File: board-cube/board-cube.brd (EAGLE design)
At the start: 100 x 100 mm, 164 parts, among them IC1 MSP430FR2110PW, IC2 LHA1+, IC3 MMZ09332BT1, Q1 BSS84, U1 TPS79933QDDCRQ1, U2 TPS79933QDDCRQ1, X1 BU-SMA-V, X10 BU-SMA-V, X11 BU-SMA-V, X12 BU-SMA-V, X13 BU-SMA-V, X14 BU-SMA-V, X15 BU-SMA-V, X16 BU-SMA-V, X17 BU-SMA-V, X2 BU-SMA-V, X3 BU-SMA-V, X4 BU-SMA-V, X5 BU-SMA-V, X6 BU-SMA-V, X7 BU-SMA-V, X8 BU-SMA-V, X9 BU-SMA-V

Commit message: adding tcxo and temp sensor
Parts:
- added C76, C77: 10n, passives-7351:C0603-N
- added C78, C79, C80, C81: 100n, passives-7351:C0603-N
- added IC4, IC5: PCT2075TP, CubeSat3:HWSON8
- added R20, R21: 4k7, passives-7351:R0603-N
- added TP4, TP5: PTR1B1,27, testpad:B1,27
- added X18, X19: SHIELD-26X26, CubeSat3:SHIELD-26X26
- added X20, X21: LFTCXO070, CubeSat3:260-SERIES
- moved C63 2.04 mm to (48.5, 24.6)
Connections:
- new net N$81: C76.1, X20.4
- new net N$82: C77.1, X21.4
- new net N$86: C78.1, C79.1, IC4.8, IC5.7, IC5.8, R20.2, R21.2
- new net SCL: IC4.2, IC5.2, R21.1, TP5.TP
- new net SDA: IC4.1, IC5.1, R20.1, TP4.TP
- net GND: now also C78.2, C79.2, C80.2, C81.2, IC4.4, IC4.5, IC4.6, IC4.7, IC4.EP, IC5.4, IC5.5, IC5.6, IC5.EP, X18.G1, X18.G10, X18.G11, X18.G12, X18.G13, X18.G14, X18.G15, X18.G16, X18.G17, X18.G19, X18.G2, X18.G20, X18.G21, X18.G3, X18.G4, X18.G5, X18.G6, X18.G7, X18.G8, X18.G9, X19.G1, X19.G10, X19.G11, X19.G12, X19.G13, X19.G14, X19.G15, X19.G16, X19.G17, X19.G19, X19.G2, X19.G20, X19.G21, X19.G3, X19.G4, X19.G5, X19.G6, X19.G7, X19.G8, X19.G9, X20.1, X20.3, X21.1, X21.3
- net N$36: now also C77.2
- net N$51: now also C80.1, X20.6
- net N$63: now also C81.1, X21.6
- net N$9: now also C76.2

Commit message: updating footprints and values, changing msp watchdog part
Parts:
- removed IC1: MSP430FR2110PW, CubeSat3:SSOP16
- removed U$1, U$4: CC1125RHBT, cube-parts:QFN50P500X500X100-32N
- added C82: (no value), passives-7351:C0603-N
- added IC6: MSP430FR2311PW, CubeSat3:SSOP16
- added IC7, IC8: CC1125RHBT, cube-parts:QFN32_5X5
- added JP11: FTDI_BASICPTH, SparkFun-Connectors:FTDI_BASIC
- added JP8: (no value), SparkFun-Connectors:1X04
- added L21: 15n, passives-7351:L0603-N
- C60: value (none) -> 12p
- moved X1 18.9 mm to (23.1, 37.8)
- moved C21 8.94 mm to (19.2, 27.4), turned to 0 degrees
- moved L4 6.45 mm to (19.2, 29.0), turned to 0 degrees
- moved C19 5.98 mm to (22.9, 25.9), turned to 0 degrees
- moved C22 5.38 mm to (17.0, 25.2), turned to 90 degrees
- moved C18 3.95 mm to (22.9, 24.2), turned to 0 degrees
- moved L3 2.88 mm to (16.0, 27.4), turned to 0 degrees
- moved X20 2.00 mm to (4.40, 9.60)
- moved C1 2.00 mm to (9.25, 21.8)
- moved C10 2.00 mm to (13.8, 9.25)
- moved C11 2.00 mm to (11.2, 10.0)
- moved C12 2.00 mm to (4.00, 12.0)
- moved C13 2.00 mm to (4.00, 13.5)
- moved C14 2.00 mm to (10.8, 21.8)
- moved C15 2.00 mm to (4.00, 15.0)
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- renumbered U$3 to FL1, U$6 to FL2, U$7 to FL3
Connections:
- new net N$83: IC6.3, JP8.4
- new net N$84: IC6.4, JP8.3
- new net N$85: IC6.11, JP11.TXO
- new net N$87: IC6.10, JP11.RXI
- new net N$88: C82.1, L21.2
- new net N$89: L21.1
- new net N$90: C82.2
- net GND: now also IC6.6, IC7.19, IC7.20, IC7.30, IC7.33, IC8.30, IC8.33, JP11.GND, JP8.2; no longer IC1.6, U$1.19, U$1.20, U$1.30, U$1.33, U$4.30, U$4.33
- net N$1: now also IC7.23; no longer U$1.23
- net N$13: now also IC7.18; no longer U$1.18
- net N$19: now also IC7.6; no longer U$1.6
- net N$2: now also IC7.24; no longer U$1.24
- net N$21: now also C60.2
- net N$30: now also IC8.23; no longer U$4.23
- net N$31: now also IC8.24; no longer U$4.24
- net N$32: now also IC8.21; no longer U$4.21
- net N$35: now also IC8.14; no longer U$4.14
- net N$36: now also IC8.32; no longer U$4.32
- net N$4: now also IC7.21; no longer U$1.21
- net N$45: now also IC8.6; no longer U$4.6
- net N$47: now also IC8.19; no longer U$4.19
- net N$48: now also IC8.20; no longer U$4.20
- net N$51: now also IC7.1, IC7.12, IC7.13, IC7.15, IC7.22, IC7.25, IC7.26, IC7.27, IC7.28, IC7.29, IC7.5; no longer U$1.1, U$1.12, U$1.13, U$1.15, U$1.22, U$1.25, U$1.26, U$1.27, U$1.28, U$1.29, U$1.5
- net N$63: now also IC8.1, IC8.12, IC8.13, IC8.15, IC8.22, IC8.25, IC8.26, IC8.27, IC8.28, IC8.29, IC8.5; no longer U$4.1, U$4.12, U$4.13, U$4.15, U$4.22, U$4.25, U$4.26, U$4.27, U$4.28, U$4.29, U$4.5
- net N$7: now also IC7.17; no longer U$1.17
- net N$8: now also IC7.14; no longer U$1.14
- net N$80: now also IC6.5, JP8.1; no longer IC1.5
- net N$9: now also IC7.32; no longer U$1.32
- net RX_CLK: now also IC8.8; no longer U$4.8
- net RX_CS: now also IC8.11; no longer U$4.11
- net RX_GPIO0: now also IC8.10; no longer U$4.10
- net RX_GPIO2: now also IC8.4; no longer U$4.4
- net RX_GPIO3: now also IC8.3; no longer U$4.3
- net RX_MISO: now also IC8.9; no longer U$4.9
- net RX_MOSI: now also IC8.7; no longer U$4.7
- net RX_RST: now also IC8.2; no longer U$4.2
- net SCL: now also IC6.15
- net SDA: now also IC6.16
- net TX_CLK: now also IC7.8; no longer U$1.8
- net TX_CS: now also IC7.11; no longer U$1.11
- net TX_GPIO0: now also IC7.10; no longer U$1.10
- net TX_GPIO2: now also IC7.4; no longer U$1.4
- net TX_GPIO3: now also IC7.3; no longer U$1.3
- net TX_MISO: now also IC7.9; no longer U$1.9
- net TX_MOSI: now also IC7.7; no longer U$1.7
- net TX_RST: now also IC7.2; no longer U$1.2
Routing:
- net TX_MISO: track 22.2 -> 20.2 mm
- net TX_GPIO3: track 30.3 -> 28.3 mm
- net TX_CLK: track 58.3 -> 56.3 mm
- net TX_GPIO0: track 23.8 -> 21.8 mm
- net GND: track 11.6 -> 12.9 mm
- net N$22: track 5.71 -> 4.68 mm
- net N$23: track 11.7 -> 12.3 mm

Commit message: added level shifter
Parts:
- removed JP10: (no value), SparkFun-Connectors:2X3
- added C83, C84, C85, C86: 100n, passives-7351:C0603-N
- added IC1, IC9: TXB0108PW, cube-parts:TSSOP20
- added JP12, JP13: M02PTH, SparkFun-Connectors:1X02
- added R22, R23: 10k, passives-7351:R0603-N
- added R24: 0.2, passives-7351:R0603-N
- JP9: value (none) -> M02PTH; device SparkFun-Connectors:2X3 -> SparkFun-Connectors:1X02
- moved JP9 633.8 mm to (-299.6, -501.2), turned to 0 degrees
- moved X12 10.1 mm to (60.8, 64.6)
- moved FL3 10.1 mm to (50.5, 64.8)
- moved X11 10.0 mm to (41.2, 64.8)
- moved R4 7.64 mm to (21.9, 63.5)
- moved Q1 6.85 mm to (18.4, 63.8)
- moved C55 4.88 mm to (16.2, 69.3)
- moved C54 4.66 mm to (16.2, 66.9)
- moved X9 2.83 mm to (89.8, 76.2)
- moved X10 2.40 mm to (69.9, 76.6)
- moved FL2 2.00 mm to (80.0, 76.3)
- moved X5 1.60 mm to (51.9, 76.6)
- moved FL1 1.26 mm to (41.4, 77.0)
- moved X3 0.89 mm to (30.5, 77.0)
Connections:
- removed net A0_CLK: JP9.3
- removed net A0_CS: JP9.1
- removed net A0_SIMO: JP9.5
- removed net B0_CLK: JP10.3
- removed net B0_CS: JP10.1
- removed net B0_SIMO: JP10.5
- new net N$91: IC9.10, JP13.1, R23.1
- new net N$92: C84.1, IC1.19
- new net N$93: C86.1, IC9.19
- new net N$94: C49.1, JP9.2, R24.2, U1.1, U1.3
- net +5V: now also JP9.1, R24.1; no longer C49.1, U1.1, U1.3
- net GND: now also C83.2, C84.2, C85.2, C86.2, IC1.11, IC9.11, JP12.2, JP13.2
- net N$51: now also C73.1, C74.1, C75.1, C83.1, IC1.2, IC6.5, JP8.1, R22.2
- net N$63: now also C85.1, IC9.2, R23.2
- net N$80: now also IC1.10, JP12.1, R22.1; no longer C73.1, C74.1, C75.1, IC6.5, JP8.1
- net RX_CLK: no longer JP10.4
- net RX_CS: no longer JP10.2
- net RX_MOSI: no longer JP10.6
- net SCL: no longer IC6.15
- net SDA: no longer IC6.16
- net TX_CLK: no longer JP9.4
- net TX_CS: no longer JP9.2
- net TX_MOSI: no longer JP9.6
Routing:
- net TX_CS: track 53.8 -> 19.6 mm
- net N$94: track 0.00 -> 2.75 mm
- net +5V: track 2.75 -> 0.00 mm

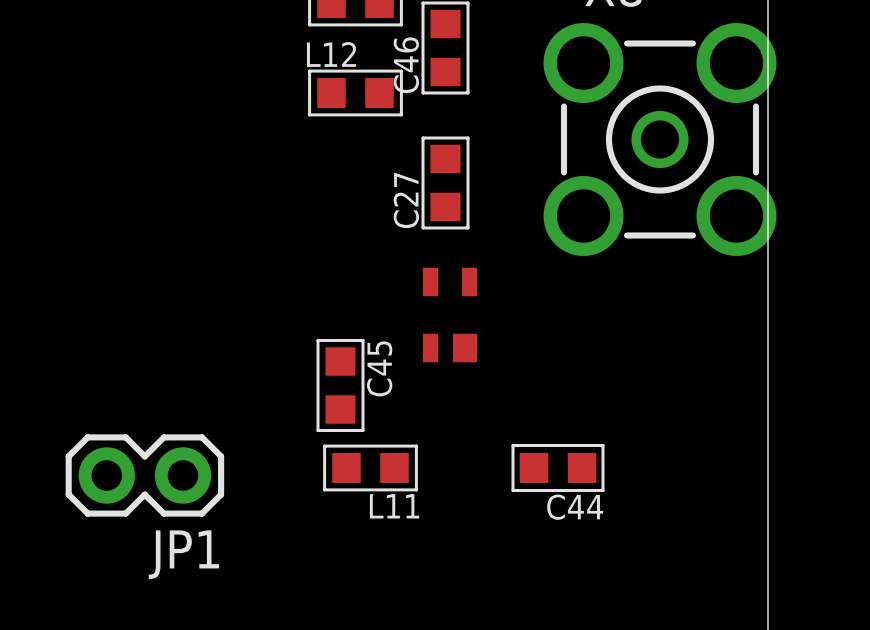
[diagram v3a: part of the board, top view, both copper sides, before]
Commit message: Fix PSA5043 LNA footprint.
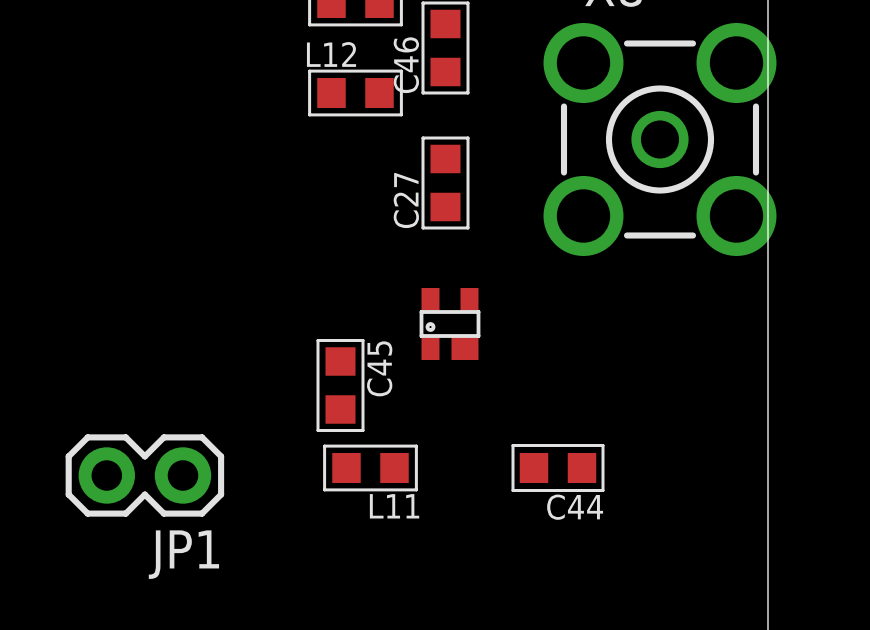
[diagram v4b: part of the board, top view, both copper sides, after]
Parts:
- renumbered U$5 to IC10
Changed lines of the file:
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@@
 <element name="L9" library="passives-7351" package="L0603-N" value="27u" x="91" y="27.25" rot="R90"/>
 <element name="C44" library="passives-7351" package="C0603-N" value="??" x="93" y="51.25" rot="R180"/>
-<element name="U$5" library="CubeSat3" package="LNA_MMM1362" value="LNA_COMMON" x="88.75" y="55.25"/>
+<element name="IC10" library="CubeSat3" package="LNA_MMM1362" value="LNA_COMMON" x="88.75" y="55.25"/>
 <element name="C27" library="passives-7351" package="C0603-N" value="??" x="89.25" y="60.75" rot="R90"/>
 <element name="L11" library="passives-7351" package="L0603-N" value="??" x="86.75" y="51.25" rot="R180"/>
@@
 <contactref element="C43" pad="2"/>
 <contactref element="L8" pad="1"/>
-<contactref element="U$5" pad="4"/>
-<contactref element="U$5" pad="2"/>
+<contactref element="IC10" pad="4"/>
+<contactref element="IC10" pad="2"/>
 <contactref element="C45" pad="1"/>
 <contactref element="L12" pad="1"/>
@@
 <wire x1="85.45" y1="66.75" x2="80.05" y2="72.286" width="0" layer="19" extent="1-1"/>
 <wire x1="85.45" y1="63.75" x2="85.45" y2="66.75" width="0" layer="19" extent="1-1"/>
-<wire x1="88.75" y1="57.45" x2="85.45" y2="63.75" width="0" layer="19" extent="1-1"/>
-<wire x1="89.9" y1="55.25" x2="88.75" y2="57.45" width="0" layer="19" extent="1-1"/>
-<wire x1="85.75" y1="54.8" x2="88.75" y2="57.45" width="0" layer="19" extent="1-1"/>
-<wire x1="93.8501" y1="59.6501" x2="88.75" y2="57.45" width="0" layer="19" extent="1-1"/>
+<wire x1="88.75" y1="56.85" x2="85.45" y2="63.75" width="0" layer="19" extent="1-1"/>
+<wire x1="89.9" y1="55.25" x2="88.75" y2="56.85" width="0" layer="19" extent="1-1"/>
+<wire x1="85.75" y1="54.8" x2="88.75" y2="56.85" width="0" layer="19" extent="1-1"/>
+<wire x1="93.8501" y1="59.6501" x2="88.75" y2="56.85" width="0" layer="19" extent="1-1"/>
 <wire x1="98.9499" y1="59.6501" x2="93.8501" y2="59.6501" width="0" layer="19" extent="1-1"/>
 <wire x1="98.9499" y1="64.7499" x2="98.9499" y2="59.6501" width="0" layer="19" extent="1-1"/>
@@
 <contactref element="L11" pad="1"/>
 <contactref element="C44" pad="2"/>
-<contactref element="U$5" pad="1"/>
+<contactref element="IC10" pad="1"/>
 <wire x1="87.55" y1="51.25" x2="92.2" y2="51.25" width="0" layer="19" extent="1-1"/>
 <wire x1="88.75" y1="55.25" x2="87.55" y2="51.25" width="0" layer="19" extent="1-1"/>
@@
 <signal name="N$46">
 <contactref element="C27" pad="1"/>
-<contactref element="U$5" pad="3"/>
-<wire x1="90.05" y1="57.45" x2="89.25" y2="59.95" width="0" layer="19" extent="1-1"/>
+<contactref element="IC10" pad="3"/>
+<wire x1="90.05" y1="56.85" x2="89.25" y2="59.95" width="0" layer="19" extent="1-1"/>
 </signal>
 <signal name="N$52">

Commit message: moving things around to fit better
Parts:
- moved IC9 596.1 mm to (71.2, 9.60)
- moved IC1 596.1 mm to (71.2, 17.2)
- moved X7 399.2 mm to (89.3, 82.6)
- moved C63 48.1 mm to (45.2, 72.7)
- moved C68 48.1 mm to (52.8, 64.4)
- moved C61 48.1 mm to (42.8, 66.8)
- moved C62 48.1 mm to (38.9, 69.0)
- moved C64 48.1 mm to (42.0, 58.4)
- moved C65 48.1 mm to (42.0, 60.0)
- moved C66 48.1 mm to (46.0, 63.2)
- moved C67 48.1 mm to (45.2, 60.8)
- moved C69 48.1 mm to (48.8, 60.8)
- moved IC3 48.1 mm to (47.8, 66.5)
- moved IC5 48.1 mm to (48.4, 72.8)
- moved L10 48.1 mm to (39.6, 66.8)
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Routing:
- net TX_CLK: track 56.3 -> 16.3 mm, vias 3 -> 2
- net RX_MISO: track 36.5 -> 0.00 mm, vias 1 -> 0
- net A1_TX: track 31.0 -> 0.00 mm
- net RX_MOSI: track 30.9 -> 0.00 mm, vias 2 -> 0
- net N$63: track 15.6 -> 0.00 mm
- net TX_RST: track 41.7 -> 28.5 mm
- net N$49: track 11.2 -> 0.00 mm
- net TX_GPIO0: track 21.8 -> 11.5 mm
- net RX_CS: track 8.98 -> 0.00 mm
- net N$47: track 8.18 -> 0.00 mm
- net RX_GPIO0: track 8.13 -> 0.00 mm
- net TX_CS: track 19.6 -> 11.7 mm
- net N$48: track 7.23 -> 0.00 mm
- net A1_RX: track 6.76 -> 0.00 mm
- net TX_GPIO3: track 28.3 -> 23.3 mm
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
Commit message: most digital signals wired up
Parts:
- removed X13: BU-SMA-V, con-coax:BU-SMA-V
- added C87: 100n, passives-7351:C0603-N
- added Q2: BSS123, transistor-small-signal:SOT23
- added Q3: BSS84, transistor-small-signal:SOT23
- added R25: 10k, passives-7351:R0603-N
- added R26: 100k, passives-7351:R0603-N
- added TP6: PTR1B1,27, testpad:B1,27
- added U3: 74LVC1G08, SparkFun-DigitalIC:SOT23-5
- JP5: value FTDI_BASICPTH -> M02PTH; device SparkFun-Connectors:FTDI_BASIC -> SparkFun-Connectors:1X02
- R18: value 4k7 -> 10k
- TP1, TP2, TP3: value PTR1PAD1-20 -> PTR1B1,27; device testpad:P1-20 -> testpad:B1,27
- U1, U2: value TPS79933QDDCRQ1 -> TPS79930QDDCRQ1
- moved R23 621.8 mm to (62.4, 9.20), turned to 90 degrees
- moved JP12 617.9 mm to (65.6, 15.6), turned to 90 degrees
- moved JP13 617.6 mm to (65.2, 8.00), turned to 90 degrees
- moved R22 616.6 mm to (62.8, 20.8), turned to 90 degrees
- moved JP11 615.4 mm to (94.4, 34.8), turned to 90 degrees
- moved C83 612.4 mm to (70.4, 22.8)
- moved C84 611.4 mm to (66.0, 21.6), turned to 90 degrees
- moved R24 607.6 mm to (30.0, 3.20), turned to 90 degrees
- moved C85 600.3 mm to (67.2, 3.60)
- moved C86 600.2 mm to (62.8, 3.60)
- moved JP9 599.7 mm to (27.2, 1.60), turned to 90 degrees
- moved C82 593.4 mm to (55.2, 28.8), turned to 90 degrees
- moved C79 590.3 mm to (48.4, 76.0)
- moved L21 588.2 mm to (52.4, 28.0)
- moved JP8 587.8 mm to (38.0, 51.6), turned to 180 degrees
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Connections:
- removed net +3V3: JP5.VCC
- removed net A1_RX: JP5.TXO
- removed net A1_TX: JP5.RXI
- removed net N$89: L21.1
- new net N$101: IC9.12
- new net N$102: IC1.20
- new net N$103: IC1.18
- new net N$104: IC1.17
- new net N$105: IC1.16
- new net N$106: IC1.15
- new net N$107: IC1.14
- new net N$108: IC1.13
- new net N$109: IC1.12
- new net N$110: IC9.13
- new net N$111: IC9.14
- new net N$112: IC9.15
- new net N$113: IC9.16
- new net N$114: IC9.17
- new net N$115: IC9.18
- new net N$116: IC9.20
- new net N$117: Q2.1, R18.2, U3.4
- new net WDT_ACK: IC6.13
- new net WDT_ERR: IC1.9, IC6.14
- new net WDT_PA_EN: IC6.2, TP6.TP, U3.2
- net +5V: now also JP7.1
- net GND: now also C87.2, IC3.10, Q2.2, U3.3; no longer JP5.GND
- net N$24: now also LED9.A
- net N$49: now also C82.2; no longer C31.2, L9.2
- net N$51: now also C87.1, U3.5
- net N$52: now also JP5.2
- net N$53: now also JP5.1, Q3.2, R26.2; no longer JP1.2
- net N$6: now also JP7.2
- net N$62: now also Q2.3; no longer JP7.1
- net N$69: now also C49.1, JP9.2, R24.2, R25.2, U1.1; no longer JP7.2, R18.2
- net N$75: now also JP1.2, Q3.3; no longer IC3.10
- net N$90: now also C31.2, L21.1, L9.2; no longer C82.2
- net N$94: now also R25.1; no longer C49.1, JP9.2, R24.2, U1.1
- net RX_CLK: now also IC9.7
- net RX_CS: now also IC9.8
- net RX_GPIO0: now also IC9.1; no longer TP3.TP
- net RX_GPIO2: now also IC9.3
- net RX_GPIO3: now also IC9.4, Q3.1, R26.1, TP3.TP
- net RX_MISO: now also IC9.6
- net RX_MOSI: now also IC9.5
- net RX_RST: now also IC9.9
- net TX_CLK: now also IC1.7
- net TX_CS: now also IC1.8, IC6.1
- net TX_GPIO0: now also IC1.1, IC6.15; no longer TP2.TP
- net TX_GPIO2: now also IC1.3
- net TX_GPIO3: now also TP2.TP, U3.1
- net TX_MISO: now also IC1.6
- net TX_MOSI: now also IC1.5
- net TX_RST: now also IC1.4, IC6.16
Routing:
- net N$94: track 2.75 -> 0.00 mm
- net N$69: track 0.00 -> 2.75 mm

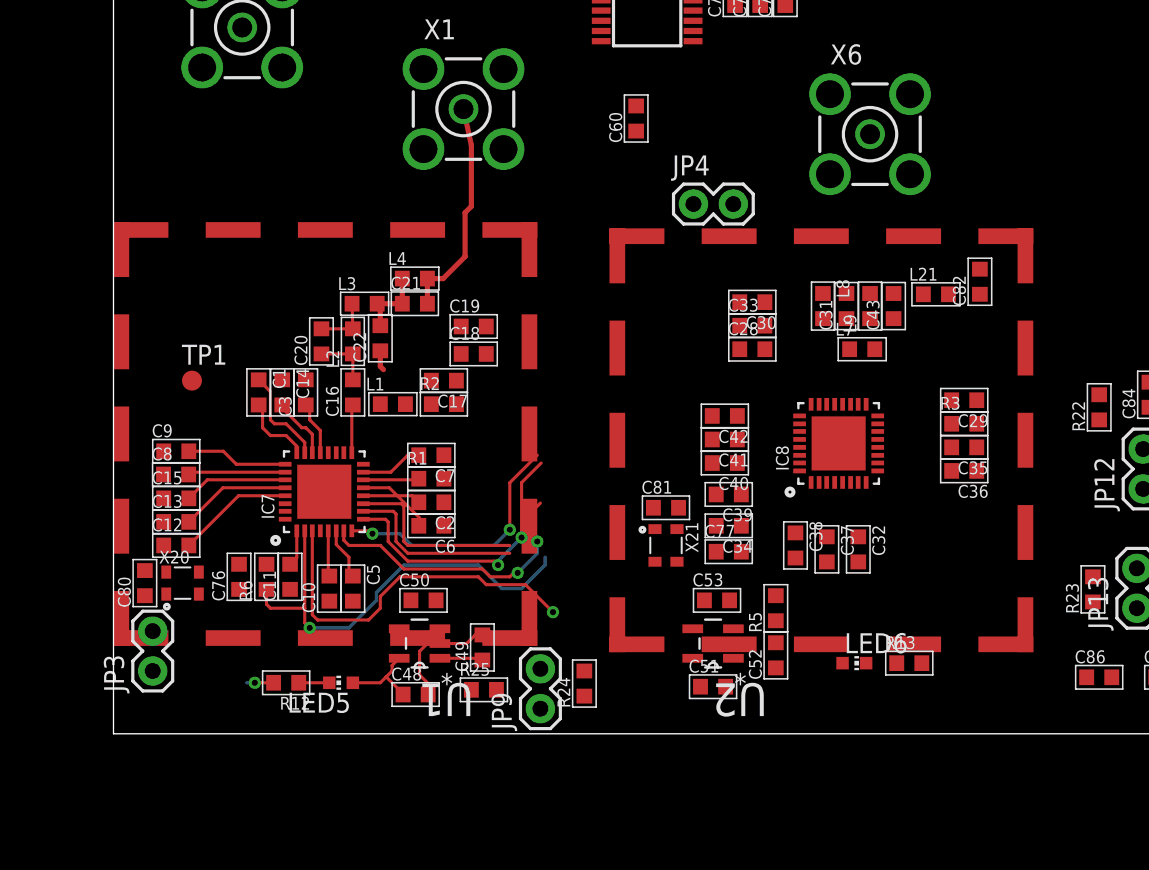
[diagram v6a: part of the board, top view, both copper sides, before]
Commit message: moving some parts around
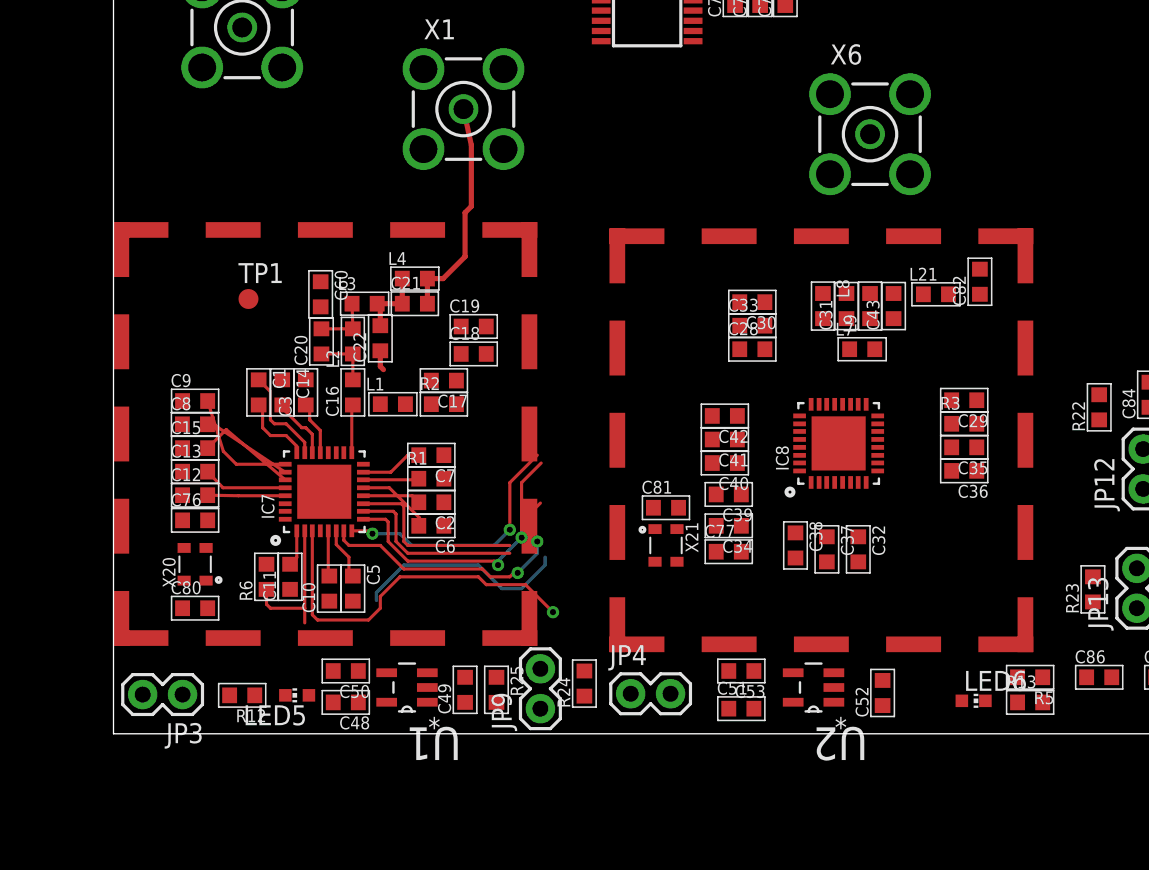
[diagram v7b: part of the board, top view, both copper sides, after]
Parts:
- moved JP4 31.5 mm to (33.0, 2.55)
- moved C60 23.0 mm to (13.2, 28.0), turned to 270 degrees
- moved R5 16.8 mm to (58.4, 3.60), turned to 180 degrees
- moved R13 8.10 mm to (58.4, 2.00)
- moved LED6 7.97 mm to (54.8, 2.10)
- moved C52 7.21 mm to (49.0, 2.60)
- moved U2 6.99 mm to (44.6, 2.95)
- moved C50 6.69 mm to (14.8, 4.00), turned to 180 degrees
- moved TP1 6.32 mm to (8.60, 27.7)
- moved C53 4.76 mm to (40.0, 4.00), turned to 180 degrees
- moved C76 4.56 mm to (5.20, 13.6), turned to 0 degrees
- moved C48 4.48 mm to (14.8, 2.00), turned to 180 degrees
- moved C80 3.58 mm to (5.20, 8.00), turned to 0 degrees
- moved C12 3.42 mm to (5.20, 15.2)
- moved C13 3.42 mm to (5.20, 16.7)
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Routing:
- net GND: track 10.4 -> 1.28 mm, vias 1 -> 0
- net TX_RST: track 28.5 -> 23.1 mm, vias 1 -> 0
- net N$39: track 5.38 -> 0.00 mm
- net N$51: track 55.6 -> 52.3 mm
- net N$69: track 2.75 -> 0.00 mm
- net N$40: track 1.95 -> 0.00 mm
